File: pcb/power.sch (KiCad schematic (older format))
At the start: 10 parts, among them P2 UNFUSED_PWR, P3 BATT, P5 BATT, U1 3v3 LDO SOT-23, U2 LD1117V33

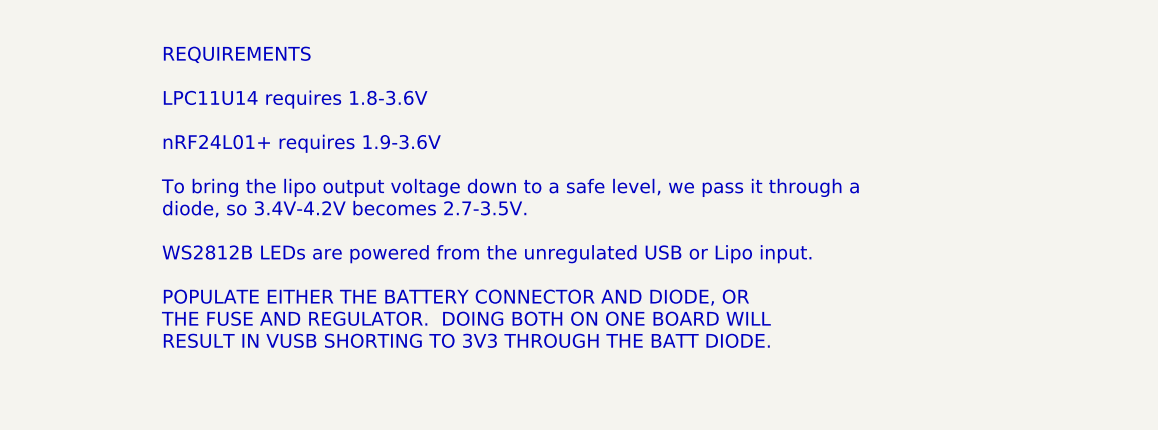
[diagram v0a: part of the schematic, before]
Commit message: added LED, and removed VLED from power sheet
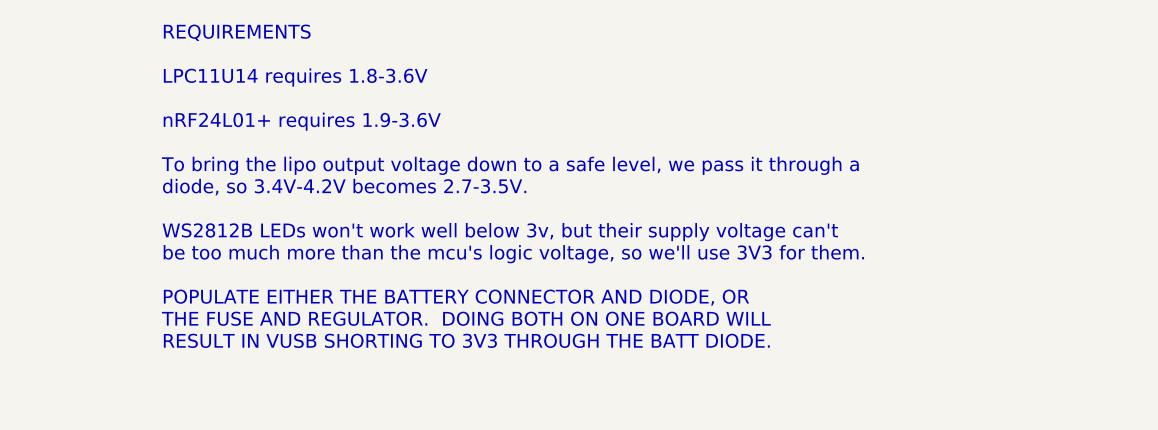
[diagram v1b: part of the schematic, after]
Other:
- note added: "REQUIREMENTS\n\nLPC11U14 requires 1.8-3.6V\n\nnRF24L01+ requires 1.9-3.6V\n\nTo bring the lipo output voltage down to a safe level, we pass it through a\ndiode, so 3.4V-4.2V becomes 2.7-3.5V.\n\nWS2812B LEDs won't work well below 3v, but their supply voltage can't\nbe too much more than the mcu's logic voltage, so we'll use 3V3 for them.\n\nPOPULATE EITHER THE BATTERY CONNECTOR AND DIODE, OR\nTHE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"
- note removed: "REQUIREMENTS\n\nLPC11U14 requires 1.8-3.6V\n\nnRF24L01+ requires 1.9-3.6V\n\nTo bring the lipo output voltage down to a safe level, we pass it through a\ndiode, so 3.4V-4.2V becomes 2.7-3.5V.\n\nWS2812B LEDs are powered from the unregulated USB or Lipo input.\n\nPOPULATE EITHER THE BATTERY CONNECTOR AND DIODE, OR\nTHE FUSE AND REGULATOR. DOING BOTH ON ONE BOARD WILL\nRESULT IN VUSB SHORTING TO 3V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"
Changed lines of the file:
@@
 $EndComp
 Text Notes 6700 1300 0    60   ~ 0
-REQUIREMENTS\n\nLPC11U14 requires 1.8-3.6V\n\nnRF24L01+ requires 1.9-3.6V\n\nTo bring the lipo output voltage down to a safe level, we pass it through a\ndiode, so 3.4V-4.2V becomes 2.7-3.5V.\n\nWS2812B LEDs are powered from the unregulated USB or Lipo input.\n\nPOPULATE EITHER THE BATTERY CONNECTOR AND DIODE, OR\nTHE FUSE AND REGULATOR.  DOING BOTH ON ONE BOARD WILL\nRESULT IN VUSB SHORTING TO 3V3 THROUGH THE BATT DIODE.
+REQUIREMENTS\n\nLPC11U14 requires 1.8-3.6V\n\nnRF24L01+ requires 1.9-3.6V\n\nTo bring the lipo output voltage down to a safe level, we pass it through a\ndiode, so 3.4V-4.2V becomes 2.7-3.5V.\n\nWS2812B LEDs won't work well below 3v, but their supply voltage can't\nbe too much more than the mcu's logic voltage, so we'll use 3V3 for them.\n\nPOPULATE EITHER THE BATTERY CONNECTOR AND DIODE, OR\nTHE FUSE AND REGULATOR.  DOING BOTH ON ONE BOARD WILL\nRESULT IN VUSB SHORTING TO 3V3 THROUGH THE BATT DIODE.
 $Comp
 L DIODE D1

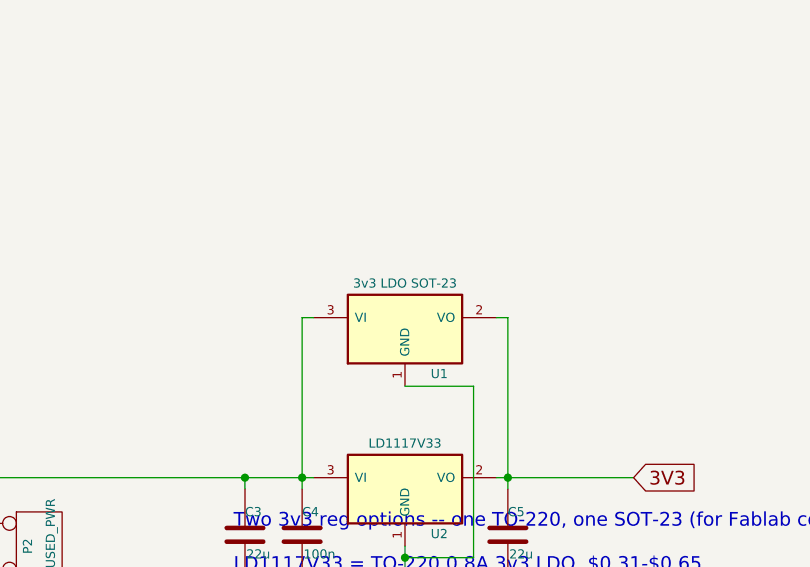
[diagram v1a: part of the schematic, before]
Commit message: gpios and rf24 connections
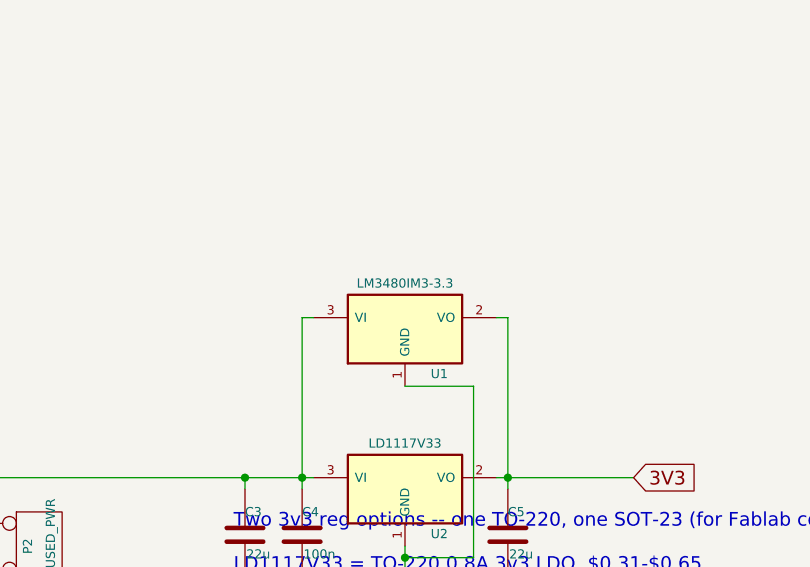
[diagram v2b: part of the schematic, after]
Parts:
- U1: value 3v3 LDO SOT-23 -> LM3480IM3-3.3
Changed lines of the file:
@@
 P 6950 3650
 F 0 "U1" H 7100 3454 40  0000 C CNN
-F 1 "3v3 LDO SOT-23" H 6950 3850 40  0000 C CNN
+F 1 "LM3480IM3-3.3" H 6950 3850 40  0000 C CNN
 F 2 "~" H 6950 3650 60  0000 C CNN
 F 3 "~" H 6950 3650 60  0000 C CNN
